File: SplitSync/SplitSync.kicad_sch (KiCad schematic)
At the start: 0 parts

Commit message: oops
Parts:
- added J1, J2: Jack-DC, symbol Connector:Jack-DC
- added SW1, SW2: Switch, symbol ScottoKeebs:Placeholder_Switch
- added U1, U3: RP2040_Zero, ScottoKeebs_MCU:RP2040_Zero, symbol ScottoKeebs:MCU_RP2040_Zero

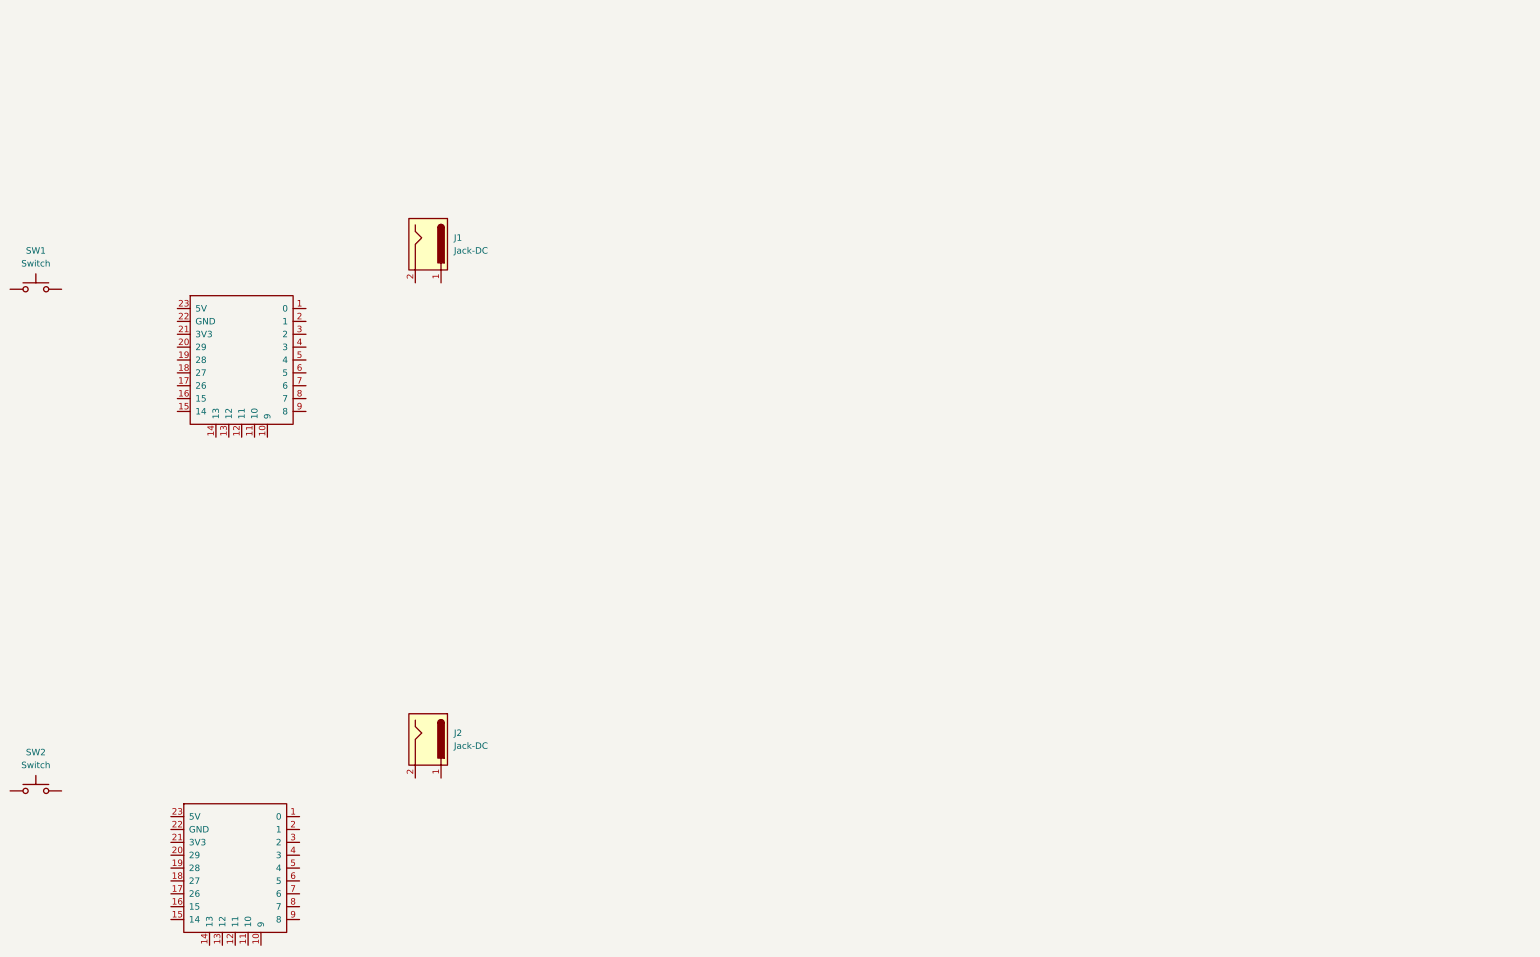
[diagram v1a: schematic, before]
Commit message: schematic for keyboard switches layout done.
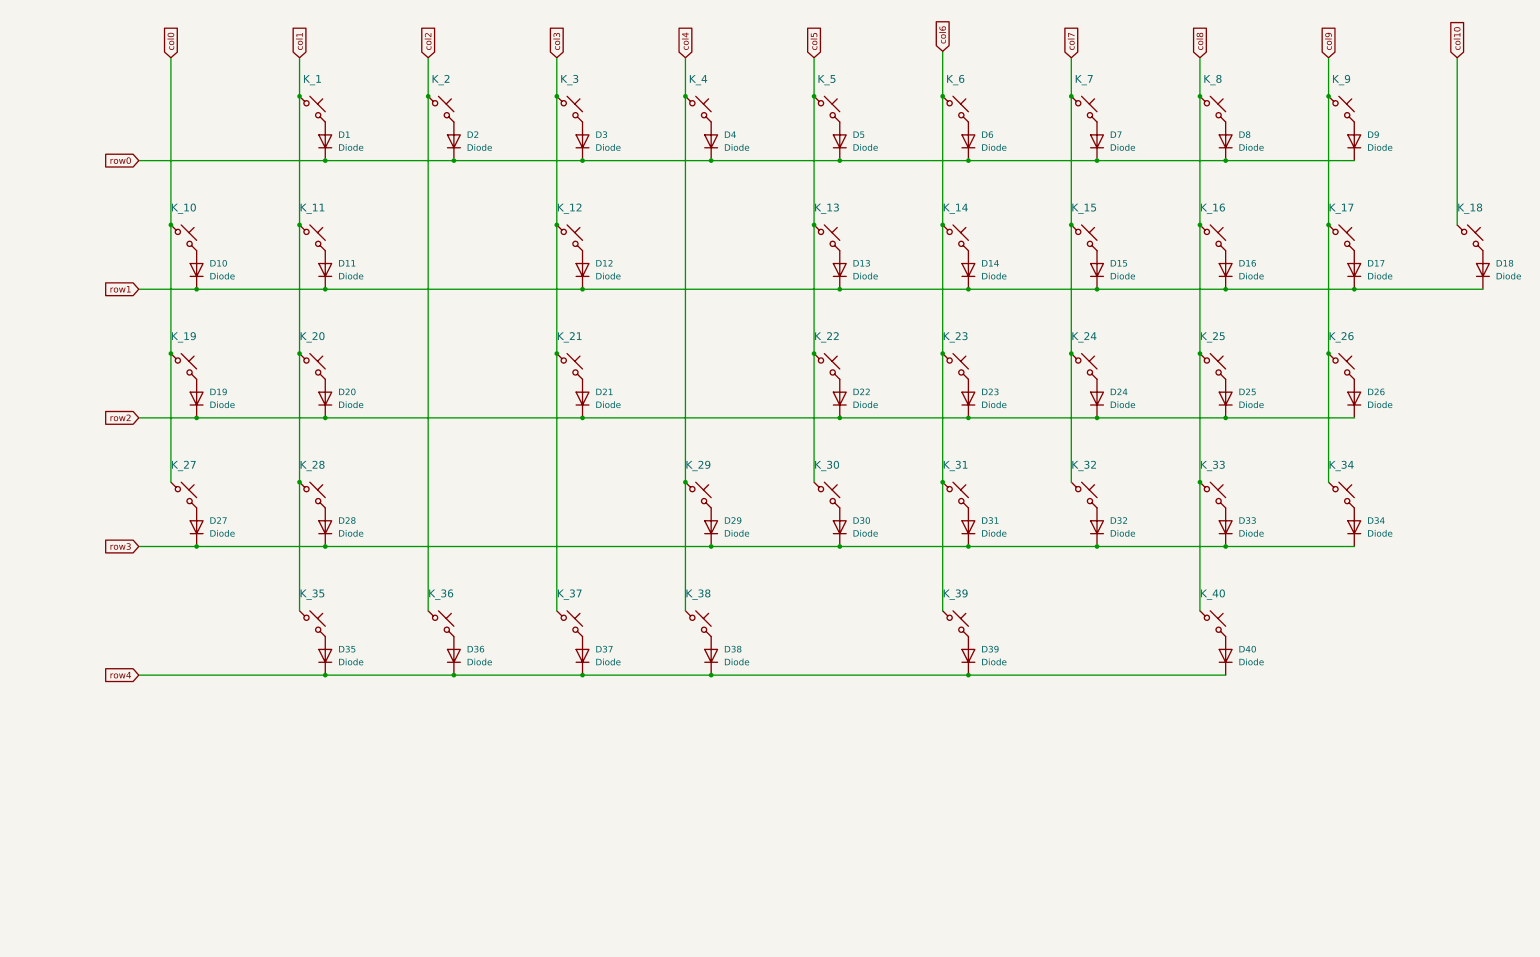
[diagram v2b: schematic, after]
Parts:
- removed J1, J2: Jack-DC, symbol Connector:Jack-DC
- removed SW1, SW2: Switch, symbol ScottoKeebs:Placeholder_Switch
- removed U1, U3: RP2040_Zero, ScottoKeebs_MCU:RP2040_Zero, symbol ScottoKeebs:MCU_RP2040_Zero
- added D1, D10, D11, D12, D13, D14, D15, D16, D17, D18, D19, D2, D20, D21, D22, D23, D24, D25, D26, D27, D28, D29, D3, D30, D31, D32, D33, D34, D35, D36, D37, D38, D39, D4, D40, D5, D6, D7, D8, D9: Diode, ScottoKeebs_Components:Diode_SOD-123, symbol ScottoKeebs:Placeholder_Diode
- added K_1, K_10, K_11, K_12, K_13, K_14, K_15, K_16, K_17, K_18, K_19, K_2, K_20, K_21, K_22, K_23, K_24, K_26, K_27, K_28, K_29, K_3, K_30, K_31, K_32, K_34, K_35, K_38, K_5, K_6, K_7, K_8, K_9: KEYSW, ScottoKeebs_Hotswap:Hotswap_MX_Plated_1.00u, symbol ScottoKeebs:Placeholder_Keyswitch
- added K_25: KEYSW, ScottoKeebs_Hotswap:Hotswap_MX_Plated_1.75u, symbol ScottoKeebs:Placeholder_Keyswitch
- added K_33: KEYSW, ScottoKeebs_Hotswap:Hotswap_MX_Plated_3.00u, symbol ScottoKeebs:Placeholder_Keyswitch
- added K_36, K_39, K_40: KEYSW, ScottoKeebs_Hotswap:Hotswap_MX_Plated_1.25u, symbol ScottoKeebs:Placeholder_Keyswitch
- added K_37: KEYSW, ScottoKeebs_Hotswap:Hotswap_MX_Plated_2.25u, symbol ScottoKeebs:Placeholder_Keyswitch
- added K_4: KEYSW, ScottoKeebs_Hotswap:Hotswap_MX_Plated_1.50u, symbol ScottoKeebs:Placeholder_Keyswitch
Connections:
- new net: D19.2 (A), K_19.2
- new net: D39.2 (A), K_39.2
- new net: D24.2 (A), K_24.2
- new net: D25.2 (A), K_25.2
- new net: D16.2 (A), K_16.2
- new net: D31.2 (A), K_31.2
- new net: D33.2 (A), K_33.2
- new net: D34.2 (A), K_34.2
- new net: D5.2 (A), K_5.2
- new net: D37.2 (A), K_37.2
- new net: D11.2 (A), K_11.2
- new net: D4.2 (A), K_4.2
- new net: D17.2 (A), K_17.2
- new net: D29.2 (A), K_29.2
- new net: D7.2 (A), K_7.2
- new net: D13.2 (A), K_13.2
- new net: D18.2 (A), K_18.2
- new net: D38.2 (A), K_38.2
- new net: D9.2 (A), K_9.2
- new net: D14.2 (A), K_14.2
- new net: D20.2 (A), K_20.2
- new net: D26.2 (A), K_26.2
- new net: D2.2 (A), K_2.2
- new net: D32.2 (A), K_32.2
- new net: D36.2 (A), K_36.2
- new net: D22.2 (A), K_22.2
- new net: D30.2 (A), K_30.2
- new net: D12.2 (A), K_12.2
- new net: D40.2 (A), K_40.2
- new net: D1.2 (A), K_1.2
- new net: D21.2 (A), K_21.2
- new net: D15.2 (A), K_15.2
- new net: D8.2 (A), K_8.2
- new net: D10.2 (A), K_10.2
- new net: D6.2 (A), K_6.2
- new net: D27.2 (A), K_27.2
- new net: D23.2 (A), K_23.2
- new net: D35.2 (A), K_35.2
- new net: D3.2 (A), K_3.2
- new net: D28.2 (A), K_28.2
- new net col0: K_10.1, K_19.1, K_27.1
- new net col1: K_1.1, K_11.1, K_20.1, K_28.1, K_35.1
- new net col10: K_18.1
- new net col2: K_2.1, K_36.1
- new net col3: K_12.1, K_21.1, K_3.1, K_37.1
- new net col4: K_29.1, K_38.1, K_4.1
- new net col5: K_13.1, K_22.1, K_30.1, K_5.1
- new net col6: K_14.1, K_23.1, K_31.1, K_39.1, K_6.1
- new net col7: K_15.1, K_24.1, K_32.1, K_7.1
- new net col8: K_16.1, K_25.1, K_33.1, K_40.1, K_8.1
- new net col9: K_17.1, K_26.1, K_34.1, K_9.1
- new net row0: D1.1 (K), D2.1 (K), D3.1 (K), D4.1 (K), D5.1 (K), D6.1 (K), D7.1 (K), D8.1 (K), D9.1 (K)
- new net row1: D10.1 (K), D11.1 (K), D12.1 (K), D13.1 (K), D14.1 (K), D15.1 (K), D16.1 (K), D17.1 (K), D18.1 (K)
- new net row2: D19.1 (K), D20.1 (K), D21.1 (K), D22.1 (K), D23.1 (K), D24.1 (K), D25.1 (K), D26.1 (K)
- new net row3: D27.1 (K), D28.1 (K), D29.1 (K), D30.1 (K), D31.1 (K), D32.1 (K), D33.1 (K), D34.1 (K)
- new net row4: D35.1 (K), D36.1 (K), D37.1 (K), D38.1 (K), D39.1 (K), D40.1 (K)
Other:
- title: SplitSync -> (none)

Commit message: layout setup entered and footprints assigned
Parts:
- removed D1, D10, D11, D12, D13, D14, D15, D16, D17, D18, D19, D2, D20, D21, D22, D23, D24, D25, D26, D27, D28, D29, D3, D30, D31, D32, D33, D34, D35, D36, D37, D38, D39, D4, D40, D5, D6, D7, D8, D9: Diode, ScottoKeebs_Components:Diode_SOD-123, symbol ScottoKeebs:Placeholder_Diode
- removed K_1, K_10, K_11, K_12, K_13, K_14, K_15, K_16, K_17, K_18, K_19, K_2, K_20, K_21, K_22, K_23, K_24, K_26, K_27, K_28, K_29, K_3, K_30, K_31, K_32, K_34, K_35, K_38, K_5, K_6, K_7, K_8, K_9: KEYSW, ScottoKeebs_Hotswap:Hotswap_MX_Plated_1.00u, symbol ScottoKeebs:Placeholder_Keyswitch
- removed K_25: KEYSW, ScottoKeebs_Hotswap:Hotswap_MX_Plated_1.75u, symbol ScottoKeebs:Placeholder_Keyswitch
- removed K_33: KEYSW, ScottoKeebs_Hotswap:Hotswap_MX_Plated_3.00u, symbol ScottoKeebs:Placeholder_Keyswitch
- removed K_36, K_39, K_40: KEYSW, ScottoKeebs_Hotswap:Hotswap_MX_Plated_1.25u, symbol ScottoKeebs:Placeholder_Keyswitch
- removed K_37: KEYSW, ScottoKeebs_Hotswap:Hotswap_MX_Plated_2.25u, symbol ScottoKeebs:Placeholder_Keyswitch
- removed K_4: KEYSW, ScottoKeebs_Hotswap:Hotswap_MX_Plated_1.50u, symbol ScottoKeebs:Placeholder_Keyswitch
- added D_0 (x2), D_1 (x2), D_10 (x2), D_11 (x2), D_12 (x2), D_13 (x2), D_14 (x2), D_15 (x2), D_16 (x2), D_17 (x2), D_18 (x2), D_19 (x2), D_2 (x2), D_20 (x2), D_21 (x2), D_22 (x2), D_23 (x2), D_24 (x2), D_25 (x2), D_26 (x2), D_27 (x2), D_28 (x2), D_29 (x2), D_3 (x2), D_30 (x2), D_31 (x2), D_32 (x2), D_33 (x2), D_34 (x2), D_35 (x2), D_36 (x2), D_37 (x2), D_38 (x2), D_39 (x2), D_4 (x2), D_40, D_41, D_5 (x2), D_6 (x2), D_7 (x2), D_8 (x2), D_9 (x2): D, ScottoKeebs_Components:Diode_SOD-123, symbol Device:D_Small
- added K_0 (x2), K_1 (x2), K_10 (x2), K_11, K_12 (x2), K_13 (x2), K_14 (x2), K_15, K_16 (x2), K_17 (x2), K_18 (x2), K_19 (x2), K_2 (x2), K_20, K_21 (x2), K_22 (x2), K_23 (x2), K_24, K_25 (x2), K_26 (x2), K_27 (x2), K_28, K_29 (x2), K_3 (x2), K_30 (x2), K_31 (x2), K_32, K_33 (x2), K_34 (x2), K_35, K_4 (x2), K_40, K_41, K_5 (x2), K_6 (x2), K_7 (x2), K_8 (x2), K_9 (x2): KEYSW, ScottoKeebs_Hotswap:Hotswap_MX_Plated_1.00u, symbol MX_Alps_Hybrid:MX-NoLED
- added K_11, K_15, K_39: KEYSW, ScottoKeebs_Hotswap:Hotswap_MX_Plated_1.50u, symbol MX_Alps_Hybrid:MX-NoLED
- added K_20: KEYSW, ScottoKeebs_Hotswap:Hotswap_MX_Plated_1.75u, symbol MX_Alps_Hybrid:MX-NoLED
- added K_24, K_28: KEYSW, ScottoKeebs_Hotswap:Hotswap_MX_Plated_2.25u, symbol MX_Alps_Hybrid:MX-NoLED
- added K_32: KEYSW, ScottoKeebs_Hotswap:Hotswap_MX_Plated_2.75u, symbol MX_Alps_Hybrid:MX-NoLED
- added K_35, K_39: KEYSW, ScottoKeebs_Hotswap:Hotswap_MX_Plated_3.00u, symbol MX_Alps_Hybrid:MX-NoLED
- added K_36 (x2), K_37 (x2), K_38 (x2): KEYSW, ScottoKeebs_Hotswap:Hotswap_MX_Plated_1.25u, symbol MX_Alps_Hybrid:MX-NoLED
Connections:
- net col0: now also K_18.1 (COL), K_26.1 (COL), K_9.1 (COL)
- net col1: now also K_0.1 (COL), K_10.1 (COL), K_19.1 (COL), K_27.1 (COL), K_34.1 (COL)
- net col10: now also K_17.1 (COL)
- net col2: now also K_1.1 (COL), K_35.1 (COL)
- net col3: now also K_11.1 (COL), K_2.1 (COL), K_20.1 (COL), K_36.1 (COL)
- net col4: now also K_28.1 (COL), K_3.1 (COL), K_37.1 (COL)
- net col5: now also K_12.1 (COL), K_21.1 (COL), K_29.1 (COL), K_4.1 (COL)
- net col6: now also K_13.1 (COL), K_22.1 (COL), K_30.1 (COL), K_38.1 (COL), K_5.1 (COL)
- net col7: now also K_14.1 (COL), K_23.1 (COL), K_31.1 (COL), K_6.1 (COL)
- net col8: now also K_15.1 (COL), K_24.1 (COL), K_32.1 (COL), K_39.1 (COL), K_7.1 (COL)
- net col9: now also K_16.1 (COL), K_25.1 (COL), K_33.1 (COL), K_8.1 (COL)
- net row0: now also D_0.1 (K), D_1.1 (K), D_2.1 (K), D_3.1 (K), D_4.1 (K), D_5.1 (K), D_6.1 (K), D_7.1 (K), D_8.1 (K)
- net row1: now also D_10.1 (K), D_11.1 (K), D_12.1 (K), D_13.1 (K), D_14.1 (K), D_15.1 (K), D_16.1 (K), D_17.1 (K), D_9.1 (K)
- net row2: now also D_18.1 (K), D_19.1 (K), D_20.1 (K), D_21.1 (K), D_22.1 (K), D_23.1 (K), D_24.1 (K), D_25.1 (K)
- net row3: now also D_26.1 (K), D_27.1 (K), D_28.1 (K), D_29.1 (K), D_30.1 (K), D_31.1 (K), D_32.1 (K), D_33.1 (K)
- net row4: now also D_34.1 (K), D_35.1 (K), D_36.1 (K), D_37.1 (K), D_38.1 (K), D_39.1 (K)
- new net: D_8.2 (A), K_8.2 (ROW) (x2)
- new net: D_29.2 (A), K_29.2 (ROW) (x2)
- new net: D_26.2 (A), K_26.2 (ROW) (x2)
- new net: D_31.2 (A), K_31.2 (ROW) (x2)
- new net: D_1.2 (A), K_1.2 (ROW) (x2)
- new net: D_12.2 (A), K_12.2 (ROW) (x2)
- new net: D_25.2 (A), K_25.2 (ROW) (x2)
- new net: D_24.2 (A), K_24.2 (ROW) (x2)
- new net: D_35.2 (A), K_35.2 (ROW) (x2)
- new net: D_41.2 (A), K_41.2 (ROW)
- new net: D_10.2 (A), K_10.2 (ROW) (x2)
- new net: D_36.2 (A), K_36.2 (ROW) (x2)
- new net: D_4.2 (A), K_4.2 (ROW) (x2)
- new net: D_22.2 (A), K_22.2 (ROW) (x2)
- new net: D_0.2 (A), K_0.2 (ROW) (x2)
- new net: D_13.2 (A), K_13.2 (ROW) (x2)
- new net: D_28.2 (A), K_28.2 (ROW) (x2)
- new net: D_30.2 (A), K_30.2 (ROW) (x2)
- new net: D_27.2 (A), K_27.2 (ROW) (x2)
- new net: D_38.2 (A), K_38.2 (ROW) (x2)
- new net: D_14.2 (A), K_14.2 (ROW) (x2)
- new net: D_39.2 (A), K_39.2 (ROW) (x2)
- new net: D_21.2 (A), K_21.2 (ROW) (x2)
- new net: D_7.2 (A), K_7.2 (ROW) (x2)
- new net: D_19.2 (A), K_19.2 (ROW) (x2)
- new net: D_37.2 (A), K_37.2 (ROW) (x2)
- new net: D_32.2 (A), K_32.2 (ROW) (x2)
- new net: D_18.2 (A), K_18.2 (ROW) (x2)
- new net: D_5.2 (A), K_5.2 (ROW) (x2)
- new net: D_11.2 (A), K_11.2 (ROW) (x2)
- new net: D_33.2 (A), K_33.2 (ROW) (x2)
- new net: D_34.2 (A), K_34.2 (ROW) (x2)
- new net: D_3.2 (A), K_3.2 (ROW) (x2)
- new net: D_15.2 (A), K_15.2 (ROW) (x2)
- new net: D_9.2 (A), K_9.2 (ROW) (x2)
- new net: D_20.2 (A), K_20.2 (ROW) (x2)
- new net: D_17.2 (A), K_17.2 (ROW) (x2)
- new net: D_6.2 (A), K_6.2 (ROW) (x2)
- new net: D_23.2 (A), K_23.2 (ROW) (x2)
- new net: D_16.2 (A), K_16.2 (ROW) (x2)
- new net: D_40.2 (A), K_40.2 (ROW)
- new net: D_2.2 (A), K_2.2 (ROW) (x2)
- new net col11: K_0.1 (COL), K_18.1 (COL)
- new net col12: K_1.1 (COL), K_19.1 (COL), K_27.1 (COL), K_35.1 (COL), K_9.1 (COL)
- new net col13: K_10.1 (COL), K_2.1 (COL), K_20.1 (COL), K_28.1 (COL)
- new net col14: K_11.1 (COL), K_21.1 (COL), K_29.1 (COL), K_3.1 (COL), K_36.1 (COL)
- new net col15: K_12.1 (COL), K_22.1 (COL), K_30.1 (COL), K_37.1 (COL), K_4.1 (COL)
- new net col16: K_13.1 (COL), K_23.1 (COL), K_31.1 (COL), K_5.1 (COL)
- new net col17: K_14.1 (COL), K_32.1 (COL), K_38.1 (COL)
- new net col18: K_15.1 (COL), K_24.1 (COL), K_39.1 (COL), K_6.1 (COL)
- new net col19: K_16.1 (COL), K_25.1 (COL), K_33.1 (COL), K_40.1 (COL), K_7.1 (COL)
- new net col20: K_17.1 (COL), K_26.1 (COL), K_34.1 (COL), K_41.1 (COL), K_8.1 (COL)
- new net row5: D_0.1 (K), D_1.1 (K), D_2.1 (K), D_3.1 (K), D_4.1 (K), D_5.1 (K), D_6.1 (K), D_7.1 (K), D_8.1 (K)
- new net row6: D_10.1 (K), D_11.1 (K), D_12.1 (K), D_13.1 (K), D_14.1 (K), D_15.1 (K), D_16.1 (K), D_17.1 (K), D_9.1 (K)
- new net row7: D_18.1 (K), D_19.1 (K), D_20.1 (K), D_21.1 (K), D_22.1 (K), D_23.1 (K), D_24.1 (K), D_25.1 (K), D_26.1 (K)
- new net row8: D_27.1 (K), D_28.1 (K), D_29.1 (K), D_30.1 (K), D_31.1 (K), D_32.1 (K), D_33.1 (K), D_34.1 (K)
- new net row9: D_35.1 (K), D_36.1 (K), D_37.1 (K), D_38.1 (K), D_39.1 (K), D_40.1 (K), D_41.1 (K)
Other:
- note added: "Left side"
- note added: "Right side"

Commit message: components laid out.
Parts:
- removed D_0 (x2), D_1 (x2), D_10 (x2), D_11 (x2), D_12 (x2), D_13 (x2), D_14 (x2), D_15 (x2), D_16 (x2), D_17 (x2), D_18 (x2), D_19 (x2), D_2 (x2), D_20 (x2), D_21 (x2), D_22 (x2), D_23 (x2), D_24 (x2), D_25 (x2), D_26 (x2), D_27 (x2), D_28 (x2), D_29 (x2), D_3 (x2), D_30 (x2), D_31 (x2), D_32 (x2), D_33 (x2), D_34 (x2), D_35 (x2), D_36 (x2), D_37 (x2), D_38 (x2), D_39 (x2), D_4 (x2), D_5 (x2), D_6 (x2), D_7 (x2), D_8 (x2), D_9 (x2): D, ScottoKeebs_Components:Diode_SOD-123, symbol Device:D_Small
- removed K_0 (x2), K_1 (x2), K_10 (x2), K_11, K_12 (x2), K_13 (x2), K_14 (x2), K_15, K_16 (x2), K_17 (x2), K_18 (x2), K_19 (x2), K_2 (x2), K_20, K_21 (x2), K_22 (x2), K_23 (x2), K_24, K_25 (x2), K_26 (x2), K_27 (x2), K_28, K_29 (x2), K_3 (x2), K_30 (x2), K_31 (x2), K_32, K_33 (x2), K_34 (x2), K_35, K_4 (x2), K_5 (x2), K_6 (x2), K_7 (x2), K_8 (x2), K_9 (x2): KEYSW, ScottoKeebs_Hotswap:Hotswap_MX_Plated_1.00u, symbol MX_Alps_Hybrid:MX-NoLED
- removed K_11, K_15, K_39: KEYSW, ScottoKeebs_Hotswap:Hotswap_MX_Plated_1.50u, symbol MX_Alps_Hybrid:MX-NoLED
- removed K_20: KEYSW, ScottoKeebs_Hotswap:Hotswap_MX_Plated_1.75u, symbol MX_Alps_Hybrid:MX-NoLED
- removed K_24, K_28: KEYSW, ScottoKeebs_Hotswap:Hotswap_MX_Plated_2.25u, symbol MX_Alps_Hybrid:MX-NoLED
- removed K_32: KEYSW, ScottoKeebs_Hotswap:Hotswap_MX_Plated_2.75u, symbol MX_Alps_Hybrid:MX-NoLED
- removed K_35, K_39: KEYSW, ScottoKeebs_Hotswap:Hotswap_MX_Plated_3.00u, symbol MX_Alps_Hybrid:MX-NoLED
- removed K_36 (x2), K_37 (x2), K_38 (x2): KEYSW, ScottoKeebs_Hotswap:Hotswap_MX_Plated_1.25u, symbol MX_Alps_Hybrid:MX-NoLED
- added D_0, D_1, D_10, D_11, D_12, D_13, D_14, D_15, D_16, D_17, D_18, D_19, D_2, D_20, D_21, D_22, D_23, D_24, D_25, D_26, D_27, D_28, D_29, D_3, D_30, D_31, D_32, D_33, D_34, D_35, D_36, D_37, D_38, D_39, D_4, D_42, D_43, D_44, D_45, D_46, D_47, D_48, D_49, D_5, D_50, D_51, D_52, D_53, D_54, D_55, D_56, D_57, D_58, D_59, D_6, D_60, D_61, D_62, D_63, D_64, D_65, D_66, D_67, D_68, D_69, D_7, D_70, D_71, D_72, D_73, D_74, D_75, D_76, D_77, D_78, D_79, D_8, D_80, D_81, D_9: D, Diode_SMD:D_SOD-123, symbol Device:D_Small
- added K_0, K_1, K_10, K_11, K_12, K_13, K_14, K_15, K_16, K_17, K_18, K_19, K_2, K_21, K_22, K_23, K_24, K_25, K_26, K_27, K_28, K_29, K_3, K_30, K_31, K_32, K_34, K_35, K_36, K_37, K_39, K_4, K_42, K_43, K_44, K_45, K_46, K_47, K_48, K_49, K_5, K_51, K_52, K_53, K_54, K_56, K_57, K_58, K_59, K_6, K_60, K_61, K_62, K_63, K_64, K_65, K_67, K_68, K_69, K_7, K_70, K_8, K_80, K_81, K_9: KEYSW, ScottoKeebs_Hotswap:Hotswap_MX_Plated_1.00u, symbol MX_Alps_Hybrid:MX-NoLED
- added K_20, K_33, K_79: KEYSW, ScottoKeebs_Hotswap:Hotswap_MX_Plated_1.50u, symbol MX_Alps_Hybrid:MX-NoLED
- added K_38: KEYSW, ScottoKeebs_Hotswap:Hotswap_MX_Plated_1.75u, symbol MX_Alps_Hybrid:MX-NoLED
- added K_50, K_55: KEYSW, ScottoKeebs_Hotswap:Hotswap_MX_Plated_2.25u, symbol MX_Alps_Hybrid:MX-NoLED
- added K_66: KEYSW, ScottoKeebs_Hotswap:Hotswap_MX_Plated_2.75u, symbol MX_Alps_Hybrid:MX-NoLED
- added K_71, K_72, K_73, K_76, K_77, K_78: KEYSW, ScottoKeebs_Hotswap:Hotswap_MX_Plated_1.25u, symbol MX_Alps_Hybrid:MX-NoLED
- added K_74, K_75: KEYSW, ScottoKeebs_Hotswap:Hotswap_MX_Plated_3.00u, symbol MX_Alps_Hybrid:MX-NoLED
- added U1, U2: RP2040_Zero, ScottoKeebs_MCU:RP2040_Zero, symbol ScottoKeebs:MCU_RP2040_Zero
- added U3, U4: TRRS, ScottoKeebs_Components:TRRS_PJ-320A, symbol ScottoKeebs:Placeholder_TRRS
- D_40, D_41: footprint ScottoKeebs_Components:Diode_SOD-123 -> Diode_SMD:D_SOD-123
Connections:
- net col19 is gone; now on net col6: K_40.1 (COL)
- net col0: now also K_18.1 (COL), K_36.1 (COL), K_53.1 (COL)
- net col1: now also K_0.1 (COL), K_19.1 (COL), K_37.1 (COL), K_54.1 (COL), K_69.1 (COL)
- net col10: now also K_26.1 (COL)
- net col11: now also K_44.1 (COL), K_61.1 (COL), K_9.1 (COL)
- net col12: now also K_10.1 (COL), K_27.1 (COL), K_45.1 (COL), K_62.1 (COL), K_75.1 (COL)
- net col13: now also K_11.1 (COL), K_28.1 (COL), K_46.1 (COL), K_63.1 (COL)
- net col14: now also K_12.1 (COL), K_29.1 (COL), K_47.1 (COL), K_64.1 (COL), K_76.1 (COL)
- net col15: now also K_13.1 (COL), K_30.1 (COL), K_48.1 (COL), K_65.1 (COL), K_77.1 (COL)
- net col16: now also K_14.1 (COL), K_31.1 (COL), K_49.1 (COL), K_78.1 (COL)
- net col17: now also K_32.1 (COL), K_50.1 (COL), K_66.1 (COL)
- net col18: now also K_15.1 (COL), K_33.1 (COL), K_79.1 (COL)
- net col2: now also K_1.1 (COL), K_70.1 (COL)
- net col20: now also K_16.1 (COL), K_34.1 (COL), K_51.1 (COL), K_67.1 (COL), K_80.1 (COL); no longer K_41.1 (COL)
- net col3: now also K_2.1 (COL), K_20.1 (COL), K_38.1 (COL), K_71.1 (COL)
- net col4: now also K_3.1 (COL), K_55.1 (COL), K_72.1 (COL)
- net col5: now also K_21.1 (COL), K_39.1 (COL), K_4.1 (COL), K_56.1 (COL)
- net col6: now also K_22.1 (COL), K_5.1 (COL), K_57.1 (COL), K_73.1 (COL)
- net col7: now also K_41.1 (COL), K_23.1 (COL), K_58.1 (COL), K_6.1 (COL)
- net col8: now also K_24.1 (COL), K_42.1 (COL), K_59.1 (COL), K_7.1 (COL), K_74.1 (COL)
- net col9: now also K_25.1 (COL), K_43.1 (COL), K_60.1 (COL), K_8.1 (COL)
- net row0: now also D_0.1 (K), D_1.1 (K), D_2.1 (K), D_3.1 (K), D_4.1 (K), D_5.1 (K), D_6.1 (K), D_7.1 (K), D_8.1 (K)
- net row1: now also D_18.1 (K), D_19.1 (K), D_20.1 (K), D_21.1 (K), D_22.1 (K), D_23.1 (K), D_24.1 (K), D_25.1 (K), D_26.1 (K)
- net row2: now also D_40.1 (K), D_41.1 (K), D_36.1 (K), D_37.1 (K), D_38.1 (K), D_39.1 (K), D_42.1 (K), D_43.1 (K)
- net row3: now also D_53.1 (K), D_54.1 (K), D_55.1 (K), D_56.1 (K), D_57.1 (K), D_58.1 (K), D_59.1 (K), D_60.1 (K)
- net row4: now also D_69.1 (K), D_70.1 (K), D_71.1 (K), D_72.1 (K), D_73.1 (K), D_74.1 (K)
- net row5: now also D_10.1 (K), D_11.1 (K), D_12.1 (K), D_13.1 (K), D_14.1 (K), D_15.1 (K), D_16.1 (K), D_17.1 (K), D_9.1 (K)
- net row6: now also D_27.1 (K), D_28.1 (K), D_29.1 (K), D_30.1 (K), D_31.1 (K), D_32.1 (K), D_33.1 (K), D_34.1 (K), D_35.1 (K)
- net row7: now also D_44.1 (K), D_45.1 (K), D_46.1 (K), D_47.1 (K), D_48.1 (K), D_49.1 (K), D_50.1 (K), D_51.1 (K), D_52.1 (K)
- net row8: now also D_61.1 (K), D_62.1 (K), D_63.1 (K), D_64.1 (K), D_65.1 (K), D_66.1 (K), D_67.1 (K), D_68.1 (K)
- net row9: now also D_75.1 (K), D_76.1 (K), D_77.1 (K), D_78.1 (K), D_79.1 (K), D_80.1 (K), D_81.1 (K); no longer D_40.1 (K), D_41.1 (K)
- new net: D_33.2 (A), K_33.2 (ROW)
- new net: D_32.2 (A), K_32.2 (ROW)
- new net: D_11.2 (A), K_11.2 (ROW)
- new net: D_4.2 (A), K_4.2 (ROW)
- new net: D_29.2 (A), K_29.2 (ROW)
- new net: D_79.2 (A), K_79.2 (ROW)
- new net: D_35.2 (A), K_35.2 (ROW)
- new net: D_7.2 (A), K_7.2 (ROW)
- new net: D_20.2 (A), K_20.2 (ROW)
- new net: D_38.2 (A), K_38.2 (ROW)
- new net: D_17.2 (A), K_17.2 (ROW)
- new net: D_70.2 (A), K_70.2 (ROW)
- new net: D_66.2 (A), K_66.2 (ROW)
- new net: D_5.2 (A), K_5.2 (ROW)
- new net: D_39.2 (A), K_39.2 (ROW)
- new net: D_52.2 (A), K_52.2 (ROW)
- new net: D_48.2 (A), K_48.2 (ROW)
- new net: D_64.2 (A), K_64.2 (ROW)
- new net: D_24.2 (A), K_24.2 (ROW)
- new net: D_14.2 (A), K_14.2 (ROW)
- new net: D_56.2 (A), K_56.2 (ROW)
- new net: D_73.2 (A), K_73.2 (ROW)
- new net: D_50.2 (A), K_50.2 (ROW)
- new net: D_60.2 (A), K_60.2 (ROW)
- new net: D_49.2 (A), K_49.2 (ROW)
- new net: D_21.2 (A), K_21.2 (ROW)
- new net: D_65.2 (A), K_65.2 (ROW)
- new net: D_6.2 (A), K_6.2 (ROW)
- new net: D_8.2 (A), K_8.2 (ROW)
- new net: D_3.2 (A), K_3.2 (ROW)
- new net: D_62.2 (A), K_62.2 (ROW)
- new net: D_63.2 (A), K_63.2 (ROW)
- new net: D_68.2 (A), K_68.2 (ROW)
- new net: D_58.2 (A), K_58.2 (ROW)
- new net: D_31.2 (A), K_31.2 (ROW)
- new net: D_19.2 (A), K_19.2 (ROW)
- new net: D_46.2 (A), K_46.2 (ROW)
- new net: D_47.2 (A), K_47.2 (ROW)
- new net: D_36.2 (A), K_36.2 (ROW)
- new net: D_15.2 (A), K_15.2 (ROW)
- new net: D_45.2 (A), K_45.2 (ROW)
- new net: D_53.2 (A), K_53.2 (ROW)
- new net: D_75.2 (A), K_75.2 (ROW)
- new net: D_78.2 (A), K_78.2 (ROW)
- new net: D_0.2 (A), K_0.2 (ROW)
- new net: D_34.2 (A), K_34.2 (ROW)
- new net: D_67.2 (A), K_67.2 (ROW)
- new net: D_2.2 (A), K_2.2 (ROW)
- new net: D_59.2 (A), K_59.2 (ROW)
- new net: D_13.2 (A), K_13.2 (ROW)
- new net: D_77.2 (A), K_77.2 (ROW)
- new net: D_51.2 (A), K_51.2 (ROW)
- new net: D_42.2 (A), K_42.2 (ROW)
- new net: D_44.2 (A), K_44.2 (ROW)
- new net: D_1.2 (A), K_1.2 (ROW)
- new net: D_25.2 (A), K_25.2 (ROW)
- new net: D_43.2 (A), K_43.2 (ROW)
- new net: D_12.2 (A), K_12.2 (ROW)
- new net: D_81.2 (A), K_81.2 (ROW)
- new net: D_28.2 (A), K_28.2 (ROW)
- new net: D_57.2 (A), K_57.2 (ROW)
- new net: D_27.2 (A), K_27.2 (ROW)
- new net: D_23.2 (A), K_23.2 (ROW)
- new net: D_10.2 (A), K_10.2 (ROW)
- new net: D_74.2 (A), K_74.2 (ROW)
- new net: D_9.2 (A), K_9.2 (ROW)
- new net: D_80.2 (A), K_80.2 (ROW)
- new net: D_76.2 (A), K_76.2 (ROW)
- new net: D_22.2 (A), K_22.2 (ROW)
- new net: D_72.2 (A), K_72.2 (ROW)
- new net: D_54.2 (A), K_54.2 (ROW)
- new net: D_18.2 (A), K_18.2 (ROW)
- new net: D_37.2 (A), K_37.2 (ROW)
- new net: D_16.2 (A), K_16.2 (ROW)
- new net: D_69.2 (A), K_69.2 (ROW)
- new net: D_71.2 (A), K_71.2 (ROW)
- new net: D_26.2 (A), K_26.2 (ROW)
- new net: D_55.2 (A), K_55.2 (ROW)
- new net: D_61.2 (A), K_61.2 (ROW)
- new net: D_30.2 (A), K_30.2 (ROW)
- new net col21: K_17.1 (COL), K_35.1 (COL), K_52.1 (COL), K_68.1 (COL), K_81.1 (COL)
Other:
- note added: "Left Side"
- note added: "Right Side"
- note removed: "Left side"
- note removed: "Right side"

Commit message: Internalized wiring done.
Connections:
- net col0: now also U1.14 (13)
- net col1: now also U1.13 (12)
- net col10: now also U1.4 (3)
- net col11: now also U2.19 (28)
- net col12: now also U2.18 (27)
- net col13: now also U2.17 (26)
- net col14: now also U2.16 (15)
- net col15: now also U2.15 (14)
- net col16: now also U2.14 (13)
- net col17: now also U2.13 (12)
- net col18: now also U2.12 (11)
- net col2: now also U1.12 (11)
- net col20: now also U2.11 (10)
- net col21: now also U2.10 (9)
- net col3: now also U1.11 (10)
- net col4: now also U1.10 (9)
- net col5: now also U1.9 (8)
- net col6: now also U1.8 (7)
- net col7: now also U1.7 (6)
- net col8: now also U1.6 (5)
- net col9: now also U1.5 (4)
- net row0: now also U1.16 (15)
- net row1: now also U1.17 (26)
- net row2: now also U1.18 (27)
- net row3: now also U1.19 (28)
- net row4: now also U1.20 (29)
- net row5: now also U2.9 (8)
- net row6: now also U2.8 (7)
- net row7: now also U2.7 (6)
- net row8: now also U2.6 (5)
- net row9: now also U2.5 (4)
